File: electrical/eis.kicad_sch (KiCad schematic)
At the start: 53 parts

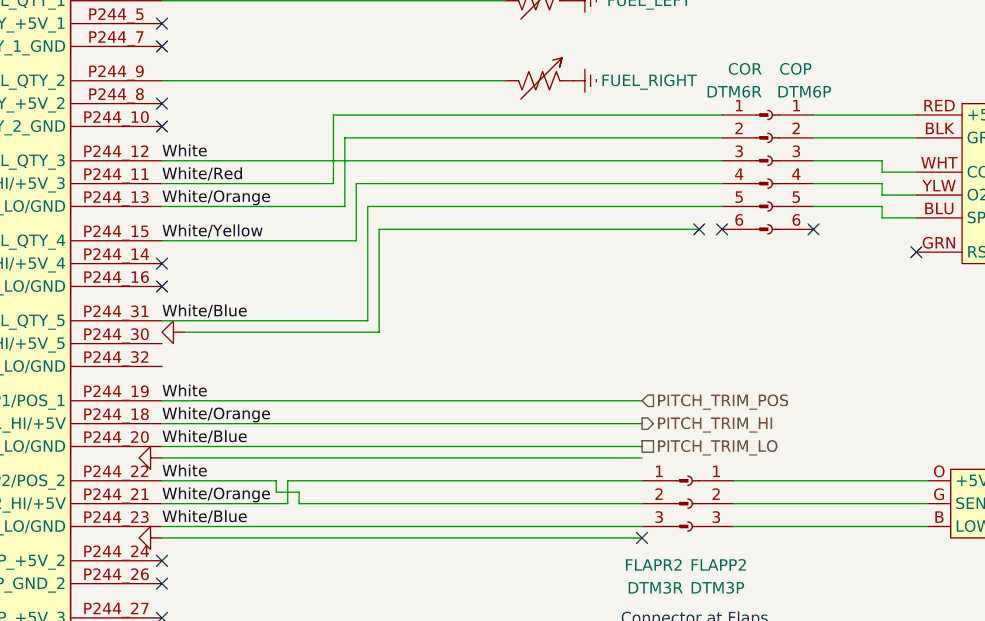
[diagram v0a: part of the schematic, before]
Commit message: Split Pitch Trim POS to go straight into connector. Changed colors on CO monitor to match what cable had. Changed colors of stick after father changed buttons.
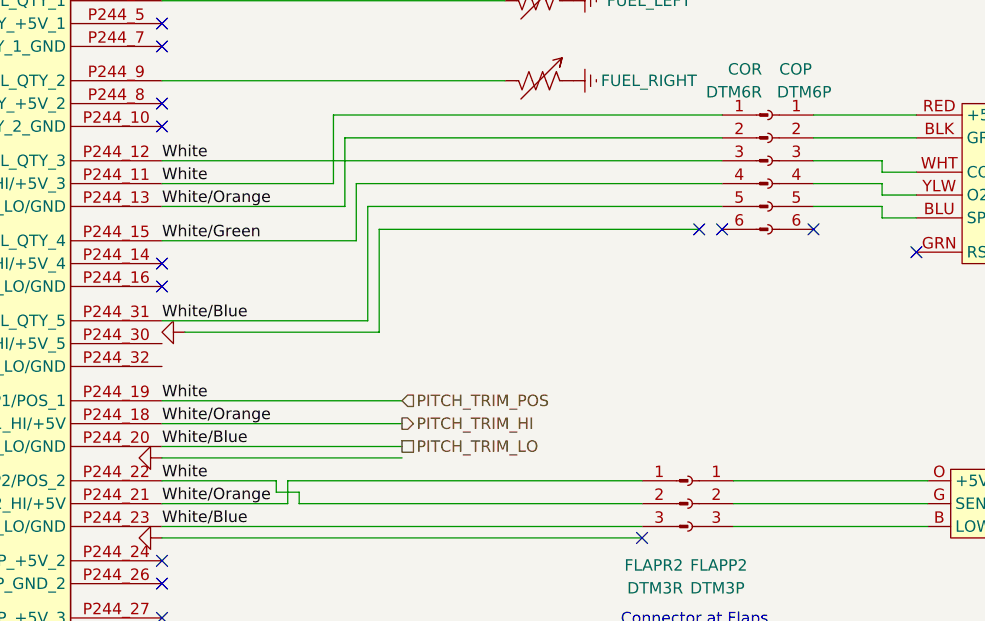
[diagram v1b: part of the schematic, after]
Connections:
- net White/Red is gone; now on net CAN_HI_IN: COR.1 (Pin_1), GEA24.P244_11 (POS_3_HI/+5V_3)
- net White/Yellow renamed White/Green
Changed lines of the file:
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@@
 	(title_block
 		(title "EIS")
-		(date "2026-01-06")
-		(rev "1.2.5")
+		(date "2026-01-15")
+		(rev "1.2.12")
 		(company "N877RV")
 	)
@@
 	(wire
 		(pts
-			(xy 67.31 280.67) (xy 120.65 280.67)
+			(xy 67.31 280.67) (xy 93.98 280.67)
 		)
 		(stroke
@@
 	(wire
 		(pts
-			(xy 67.31 275.59) (xy 120.65 275.59)
+			(xy 67.31 275.59) (xy 93.98 275.59)
 		)
 		(stroke
@@
 	(wire
 		(pts
-			(xy 67.31 281.94) (xy 120.65 281.94)
+			(xy 67.31 281.94) (xy 93.98 281.94)
 		)
 		(stroke
@@
 	(wire
 		(pts
-			(xy 67.31 278.13) (xy 120.65 278.13)
+			(xy 67.31 278.13) (xy 93.98 278.13)
 		)
 		(stroke
@@
 		)
 	)
-	(label "White{slash}Yellow"
+	(label "White{slash}Green"
 		(at 67.31 257.81 0)
 		(effects
@@
 		)
 	)
-	(label "White{slash}Red"
+	(label "White"
 		(at 67.31 251.46 0)
 		(effects
@@
 		)
 	)
-	(hierarchical_label "GEA24_PWR"
-		(shape input)
-		(at 223.52 21.59 0)
+	(hierarchical_label "PITCH_TRIM_LO"
+		(shape passive)
+		(at 93.98 280.67 0)
 		(effects
 			(font
@@
 		)
 	)
-	(hierarchical_label "PITCH_TRIM_HI"
-		(shape output)
-		(at 120.65 278.13 0)
+	(hierarchical_label "GEA24_PWR"
+		(shape input)
+		(at 223.52 21.59 0)
 		(effects
 			(font
@@
 		)
 	)
-	(hierarchical_label "PITCH_TRIM_LO"
-		(shape passive)
-		(at 120.65 280.67 0)
+	(hierarchical_label "PITCH_TRIM_POS"
+		(shape input)
+		(at 93.98 275.59 0)
 		(effects
 			(font
@@
 		)
 	)
+	(hierarchical_label "PITCH_TRIM_HI"
+		(shape output)
+		(at 93.98 278.13 0)
+		(effects
+			(font
+				(size 1.27 1.27)
+			)
+			(justify left)
+		)
+	)
 	(hierarchical_label "EIS_SERIAL_OUT"
 		(shape output)
@@
 		)
 	)
-	(hierarchical_label "PITCH_TRIM_POS"
-		(shape input)
-		(at 120.65 275.59 0)
-		(effects
-			(font
-				(size 1.27 1.27)
-			)
-			(justify left)
-		)
-	)
